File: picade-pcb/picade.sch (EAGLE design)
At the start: 41 parts

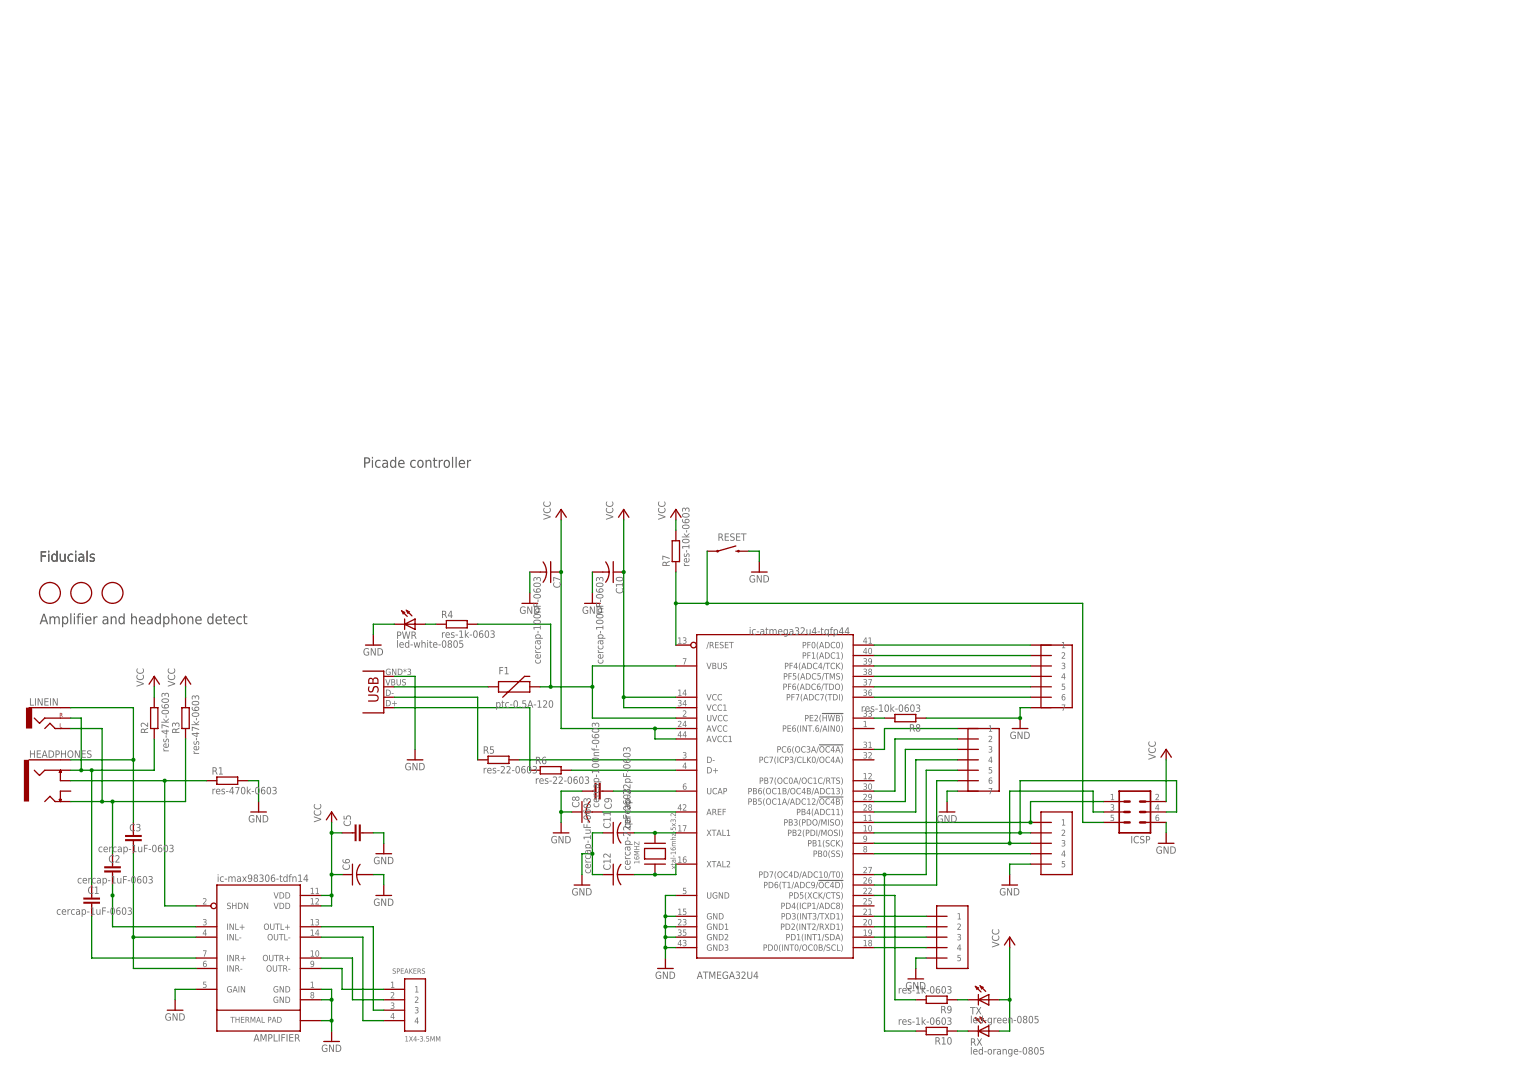
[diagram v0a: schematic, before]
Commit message: v2.00
Production revision of the Picade controller board with matrix scanned
inputs, new amplifier with I2C volume control, and extra audio
filtering.
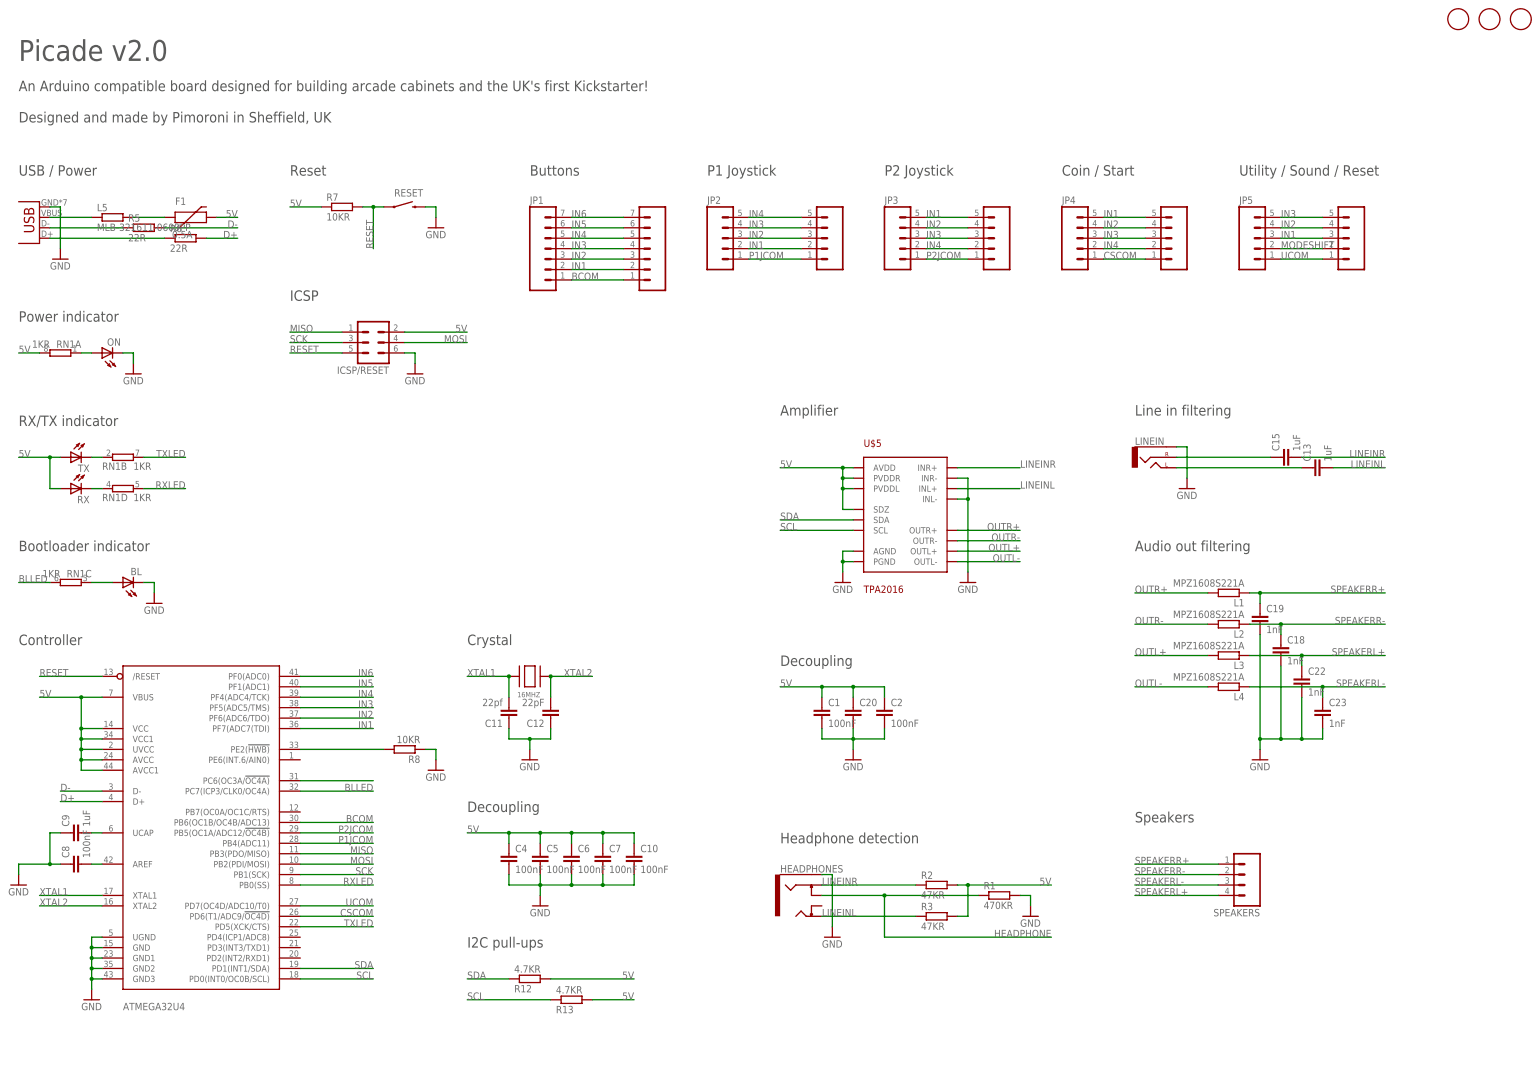
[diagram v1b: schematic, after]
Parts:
- removed AMPLIFIER: ic-max98306-tdfn14, SparkFun-PowerIC:MAX98306ETD+
- removed C3: cercap-1uF-0603, resistor:C-EUC0603K
- removed GPIO: 1X71X7, pimoroni:1X71X7
- removed ICSP: (no value), con-lstb:MA03-2
- removed JOYSTICK: 1X5, adafruit:1X5
- removed PWR: led-white-0805, adafruit:LEDCHIPLED_0805
- removed R10, R4, R9: res-1k-0603, resistor:R-EU_R0603
- added BL, ON: (no value), adafruit:LEDCHIPLED_0805
- added C13, C15: 1uF, resistor:C-EUC0603K
- added C18, C19, C22, C23: 1nF, resistor:C-EUC0603K
- added C20: (no value), resistor:C-EUC0805K
- added C4: 100nF, resistor:C-EUC0603K
- added COIN, P1JOY, P2JOY: 2.54MM-5P-SCREW-TERMINALLOCK, pimoroni:2.54MM-5P-SCREW-TERMINALLOCK
- added ICSP/RESET: (no value), con-lstb:MA03-2
- added JP1: (no value), SparkFun-Connectors:M07LOCK
- added JP2, JP3, JP4, JP5: (no value), SparkFun-Connectors:M05LOCK
- added L1, L2, L3, L4: MPZ1608S221A, resistor:R-EU_R0603
- added L5: MLB-321611-0600PP, rcl:R-EU_R1206
- added R12, R13: 4.7KR, resistor:R-EU_R0603
- added RN1: 1KR, resistor-dil:4R-N0603-ARC
- added U$5: TPA2016, pimoroni:TPA2016D2
- 16MHZ: value xtal-16mhz-5x3.2 -> (none)
- ATMEGA32U4: value ic-atmega32u4-tqfp44 -> ATMEGA32U4-AU; device adafruit:ATMEGA32U4-AU -> pimoroni:ATMEGA32U4-AU
- BUTTONS: value 1X71X7 -> 2.54MM-7P-SCREW-TERMINALLOCK; device pimoroni:1X71X7 -> pimoroni:2.54MM-7P-SCREW-TERMINALLOCK
- C1, C2: value cercap-1uF-0603 -> 100nF
- C10, C6, C7: value cercap-100nF-0603 -> 100nF; device adafruit:C-USC0603K -> resistor:C-EUC0603K
- C11: value cercap-22pF-0603 -> 22pf; device adafruit:C-USC0603K -> resistor:C-EUC0603K
- C12: value cercap-22pF-0603 -> 22pF; device adafruit:C-USC0603K -> resistor:C-EUC0603K
- C5: value cercap-10uF-0805 -> 100nF; device resistor:C-EUC0805K -> resistor:C-EUC0603K
- C8: value cercap-100nf-0603 -> 100nF; device adafruit:C-USC0603K -> resistor:C-EUC0603K
- C9: value cercap-1uF-0603 -> 1uF
- F1: value ptc-0.5A-120 -> 0.5A
- R1: value res-470k-0603 -> 470KR
- R2, R3: value res-47k-0603 -> 47KR
- R5, R6: value res-22-0603 -> 22R
- R7, R8: value res-10k-0603 -> 10KR
- RX: value led-orange-0805 -> (none)
- SPEAKERS: value 1X4-3.5MM -> 2.54MM-4P-SCREW-TERMINALLOCK; device adafruit:1X4-3.5MM -> pimoroni:2.54MM-4P-SCREW-TERMINALLOCK
- TX: value led-green-0805 -> (none)
- U$1, U$2, U$3: value FIDUCIAL -> FIDUCIAL2MM; device adafruit:FIDUCIAL -> pimoroni:FIDUCIAL2MM
- USB: value USB-REVERSE-MICROB -> USB-MICROB; device pimoroni:USB-REVERSE-MICROB -> pimoroni:USB-MICROB
- UTILITY: value 1X5 -> 2.54MM-5P-SCREW-TERMINALLOCK; device adafruit:1X5 -> pimoroni:2.54MM-5P-SCREW-TERMINALLOCK
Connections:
- net N$1 renamed XTAL1
- net N$2 renamed D-
- net N$5 renamed D+
- net N$8 renamed XTAL2
- removed net N$10: ATMEGA32U4.PD5(XCK/CTS), R9.2
- removed net N$13: ATMEGA32U4.PD7(OC4D/ADC10/T0), GPIO.5, R10.2
- removed net N$14: ATMEGA32U4.PB3(PDO/MISO), ICSP.1, JOYSTICK.1
- removed net N$16: ATMEGA32U4.PB1(SCK), ICSP.3, JOYSTICK.3
- removed net N$17: C3.1, HEADPHONES.SLEEVE, LINEIN.SLEEVE
- removed net N$18: ATMEGA32U4.PF0(ADC0), BUTTONS.1
- removed net N$19: ATMEGA32U4.PF1(ADC1), BUTTONS.2
- removed net N$20: ATMEGA32U4.PF4(ADC4/TCK), BUTTONS.3
- removed net N$21: ATMEGA32U4.PF5(ADC5/TMS), BUTTONS.4
- removed net N$22: ATMEGA32U4.PF6(ADC6/TDO), BUTTONS.5
- removed net N$23: ATMEGA32U4.PF7(ADC7(TDI), BUTTONS.6
- removed net N$24: ATMEGA32U4.PD3(INT3/TXD1), UTILITY.1
- removed net N$25: ATMEGA32U4.PD2(INT2/RXD1), UTILITY.2
- removed net N$26: ATMEGA32U4.PD1(INT1/SDA), UTILITY.3
- removed net N$27: ATMEGA32U4.PD0(INT0/OC0B/SCL), UTILITY.4
- removed net N$28: ATMEGA32U4.PB0(SS), JOYSTICK.4
- removed net N$29: ATMEGA32U4.PB5(OC1A/ADC12/!OC4B), GPIO.3
- removed net N$30: ATMEGA32U4.PB6(OC1B/OC4B/ADC13), GPIO.2
- removed net N$31: ATMEGA32U4.PC6(OC3A/!OC4A), GPIO.1
- removed net N$32: AMPLIFIER.INL-, AMPLIFIER.INR-, C3.2
- removed net N$33: ATMEGA32U4.PD6(T1/ADC9/!OC4D), GPIO.6
- removed net N$34: ATMEGA32U4.PB4(ADC11), GPIO.4
- removed net N$35: AMPLIFIER.INL+, C2.2
- removed net N$36: AMPLIFIER.INR+, C1.2
- removed net N$37: C1.1, HEADPHONES.RING, LINEIN.RIGHT, R2.1
- removed net N$38: C2.1, HEADPHONES.TIP, LINEIN.LEFT, R3.1
- removed net N$39: ATMEGA32U4.PB2(PDI/MOSI), ICSP.4, JOYSTICK.2
- removed net N$42: AMPLIFIER.SHDN, HEADPHONES.RSH, R1.1
- removed net N$9: PWR.A, R4.1
- removed net VCC: AMPLIFIER.VDD@1, AMPLIFIER.VDD@2, ATMEGA32U4.AVCC, ATMEGA32U4.AVCC1, ATMEGA32U4.UVCC, ATMEGA32U4.VBUS, ATMEGA32U4.VCC, ATMEGA32U4.VCC1, C10.1, C5.1, C6.1, C7.1, F1.2, ICSP.2, R2.2, R3.2, R4.2, R7.2, RX.A, TX.A
- new net 5V: ATMEGA32U4.AVCC, ATMEGA32U4.AVCC1, ATMEGA32U4.UVCC, ATMEGA32U4.VBUS, ATMEGA32U4.VCC, ATMEGA32U4.VCC1, C1.1, C10.1, C2.1, C20.1, C4.1, C5.1, C6.1, C7.1, F1.2, ICSP/RESET.2, R12.2, R13.2, R2.2, R3.2, R7.1, RN1A.2, RX.A, TX.A, U$5.AVDD, U$5.PVDDL, U$5.PVDDR, U$5.SDZ
- new net BCOM: ATMEGA32U4.PB6(OC1B/OC4B/ADC13), BUTTONS.1, JP1.1
- new net BLLED: ATMEGA32U4.PC7(ICP3/CLK0/OC4A), RN1C.2
- new net CSCOM: ATMEGA32U4.PD6(T1/ADC9/!OC4D), COIN.1, JP4.1
- new net HEADPHONE: ATMEGA32U4.PC6(OC3A/!OC4A), HEADPHONES.RSH, R1.1
- new net IN1: ATMEGA32U4.PF7(ADC7(TDI), BUTTONS.2, COIN.5, JP1.2, JP2.2, JP3.5, JP4.5, JP5.3, P1JOY.2, P2JOY.5, UTILITY.3
- new net IN2: ATMEGA32U4.PF6(ADC6/TDO), BUTTONS.3, COIN.4, JP1.3, JP2.3, JP3.4, JP4.4, JP5.4, P1JOY.3, P2JOY.4, UTILITY.4
- new net IN3: ATMEGA32U4.PF5(ADC5/TMS), BUTTONS.4, COIN.3, JP1.4, JP2.4, JP3.3, JP4.3, JP5.5, P1JOY.4, P2JOY.3, UTILITY.5
- new net IN4: ATMEGA32U4.PF4(ADC4/TCK), BUTTONS.5, COIN.2, JP1.5, JP2.5, JP3.2, JP4.2, P1JOY.5, P2JOY.2
- new net IN5: ATMEGA32U4.PF1(ADC1), BUTTONS.6, JP1.6
- new net IN6: ATMEGA32U4.PF0(ADC0), BUTTONS.7, JP1.7
- new net LINEINL: C13.2, HEADPHONES.TIP, R3.1, U$5.INL+
- new net LINEINR: C15.2, HEADPHONES.RING, R2.1, U$5.INR+
- new net MISO: ATMEGA32U4.PB3(PDO/MISO), ICSP/RESET.1
- new net MODESHIFT: JP5.2, UTILITY.2
- new net MOSI: ATMEGA32U4.PB2(PDI/MOSI), ICSP/RESET.4
- new net N$1: ATMEGA32U4.UCAP, C9.2
- new net N$2: ON.A, RN1A.1
- new net N$7: F1.1, L5.2
- new net P1JCOM: ATMEGA32U4.PB4(ADC11), JP2.1, P1JOY.1
- new net P2JCOM: ATMEGA32U4.PB5(OC1A/ADC12/!OC4B), JP3.1, P2JOY.1
- new net PRELINEINL: C13.1, LINEIN.LEFT
- new net PRELINEINR: C15.1, LINEIN.RIGHT
- new net RXLED: ATMEGA32U4.PB0(SS), RN1D.2
- new net SCK: ATMEGA32U4.PB1(SCK), ICSP/RESET.3
- new net SCL: ATMEGA32U4.PD0(INT0/OC0B/SCL), R13.1, U$5.SCL
- new net SDA: ATMEGA32U4.PD1(INT1/SDA), R12.1, U$5.SDA
- new net SPEAKERL+: C22.1, L3.1, SPEAKERS.4
- new net SPEAKERL-: C23.1, L4.1, SPEAKERS.3
- new net SPEAKERR+: C19.1, L1.1, SPEAKERS.1
- new net SPEAKERR-: C18.1, L2.1, SPEAKERS.2
- new net TXLED: ATMEGA32U4.PD5(XCK/CTS), RN1B.2
- new net UCOM: ATMEGA32U4.PD7(OC4D/ADC10/T0), JP5.1, UTILITY.1
- net GND: now also BL.C, C1.2, C18.2, C19.2, C2.2, C20.2, C22.2, C23.2, C4.2, C9.1, HEADPHONES.SLEEVE, ICSP/RESET.6, LINEIN.SLEEVE, ON.C, U$5.AGND, U$5.INL-, U$5.INR-, U$5.PGND; no longer AMPLIFIER.GAIN, AMPLIFIER.GND@1, AMPLIFIER.GND@2, AMPLIFIER.GND@3, BUTTONS.7, C9.2, GPIO.7, ICSP.6, JOYSTICK.5, PWR.C, UTILITY.5
- net N$11: now also RN1B.1; no longer R9.1
- net N$12: now also RN1D.1; no longer R10.1
- net N$15: now also L5.1; no longer F1.1
- net N$6: now also BL.A, RN1C.1; no longer ATMEGA32U4.UCAP, C9.1
- net OUTL+: now also L3.2, U$5.OUTL+; no longer AMPLIFIER.OUTL+, SPEAKERS.3
- net OUTL-: now also L4.2, U$5.OUTL-; no longer AMPLIFIER.OUTL-, SPEAKERS.4
- net OUTR+: now also L1.2, U$5.OUTR+; no longer AMPLIFIER.OUTR+, SPEAKERS.2
- net OUTR-: now also L2.2, U$5.OUTR-; no longer AMPLIFIER.OUTR-, SPEAKERS.1
- net RESET: now also ICSP/RESET.5, R7.2; no longer ICSP.5, R7.1
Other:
- note added: "Amplifier"
- note added: "An Arduino compatible board designed for building arcade cabinets and the UK's first Kickstarter! Designed and made by Pimoroni in Sheffield, UK"
- note added: "Audio out filtering"
- note added: "Bootloader indicator"
- note added: "Buttons"
- note added: "Coin / Start"
- note added: "Controller"
- note added: "Crystal"
- note added: "Decoupling"
- note added: "Headphone detection"
- note added: "I2C pull-ups"
- note added: "ICSP"
- note added: "Line in filtering"
- note added: "P1 Joystick"
- note added: "P2 Joystick"
- note added: "Picade v2.0"
- note added: "Power indicator"
- note added: "RX/TX indicator"
- note added: "Reset"
- note added: "Speakers"
- note added: "USB / Power"
- note added: "Utility / Sound / Reset"
- note removed: "Amplifier and headphone detect"
- note removed: "Fiducials"
- note removed: "Picade controller"
- moved on the sheet: 16MHZ, ATMEGA32U4, C1, C10, C11, C12, C2, C5, C6, C7, C8, C9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

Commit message: Picade retail board V2.01
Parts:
- U$1, U$2, U$3: value FIDUCIAL2MM -> FIDUCIAL1MM; device pimoroni:FIDUCIAL2MM -> pimoroni:FIDUCIAL1MM
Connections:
- net MODESHIFT: now also ATMEGA32U4.PD4(ICP1/ADC8)
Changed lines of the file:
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@@
 <part name="GND18" library="supply1" deviceset="GND" device=""/>
 <part name="R7" library="resistor" deviceset="R-EU_" device="R0603" value="10KR"/>
-<part name="U$3" library="pimoroni" deviceset="FIDUCIAL" device="2MM"/>
-<part name="U$1" library="pimoroni" deviceset="FIDUCIAL" device="2MM"/>
-<part name="U$2" library="pimoroni" deviceset="FIDUCIAL" device="2MM"/>
+<part name="U$3" library="pimoroni" deviceset="FIDUCIAL" device="1MM" value="FIDUCIAL1MM"/>
+<part name="U$1" library="pimoroni" deviceset="FIDUCIAL" device="1MM" value="FIDUCIAL1MM"/>
+<part name="U$2" library="pimoroni" deviceset="FIDUCIAL" device="1MM" value="FIDUCIAL1MM"/>
 <part name="R8" library="resistor" deviceset="R-EU_" device="R0603" value="10KR"/>
 <part name="HEADPHONES" library="pimoroni" deviceset="AUDIO-JACK2" device="SMD" value="stereo-jack-switched"/>
@@
 <pinref part="UTILITY" gate="G$1" pin="2"/>
 </segment>
-</net>
+<segment>
+<pinref part="ATMEGA32U4" gate="G$1" pin="PD4(ICP1/ADC8)"/>
+<wire x1="99.06" y1="27.94" x2="81.28" y2="27.94" width="0.1524" layer="91"/>
+<label x="99.06" y="27.94" size="1.778" layer="95" rot="MR0"/>
+</segment>
+</net>

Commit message: Prior to amplifier change
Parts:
- C20: value (none) -> 10uF
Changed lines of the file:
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@@
 <part name="C23" library="resistor" deviceset="C-EU" device="C0603K" value="1nF"/>
 <part name="RN1" library="resistor-dil" deviceset="4R-N" device="0603-ARC" value="1KR"/>
-<part name="C20" library="resistor" deviceset="C-EU" device="C0805K"/>
+<part name="C20" library="resistor" deviceset="C-EU" device="C0805K" value="10uF"/>
 <part name="C2" library="resistor" deviceset="C-EU" device="C0603K" value="100nF"/>
 <part name="GND13" library="supply1" deviceset="GND" device=""/>
@@
 <pinref part="ATMEGA32U4" gate="G$1" pin="PC6(OC3A/!OC4A)"/>
 <wire x1="81.28" y1="66.04" x2="99.06" y2="66.04" width="0.1524" layer="91"/>
-</segment>
-</net>
+<label x="99.06" y="66.04" size="1.778" layer="95" rot="MR0"/>
+</segment>
+</net>

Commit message: v1.02
Changed amp to allow for up/down volume control. Better USB signal
routing. Pull-up on MODESHIFT
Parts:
- removed C20: 10uF, resistor:C-EUC0805K
- removed R12, R13: 4.7KR, resistor:R-EU_R0603
- removed U$5: TPA2016, pimoroni:TPA2016D2
- added C14: 0.1uF, resistor:C-EUC0603K
- added C3: 100uF, resistor:CPOL-EU153CLV-0605
- added R4: 47KR, resistor:R-EU_R0603
- added U$4: PAM8407, pimoroni:PAM8407
- C13, C15: value 1uF -> 0.1uF
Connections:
- removed net PRELINEINL: C13.1, LINEIN.LEFT
- removed net PRELINEINR: C15.1, LINEIN.RIGHT
- removed net SCL: ATMEGA32U4.PD0(INT0/OC0B/SCL), R13.1, U$5.SCL
- removed net SDA: ATMEGA32U4.PD1(INT1/SDA), R12.1, U$5.SDA
- new net LIENINLCAP: C13.2, U$4.LINP
- new net LINEINRCAP: C15.2, U$4.RINP
- new net N$9: C14.2, U$4.LINN, U$4.RINN
- new net SHDWN: U$4.SD
- new net VDOWN: ATMEGA32U4.PD1(INT1/SDA), U$4.DOWN
- new net VUP: ATMEGA32U4.PD0(INT0/OC0B/SCL), U$4.UP
- net 5V: now also C3.+, R4.2, U$4.VDD; no longer C20.1, R12.2, R13.2, U$5.AVDD, U$5.PVDDL, U$5.PVDDR, U$5.SDZ
- net BLLED: now also RN1B.2; no longer RN1C.2
- net GND: now also C14.1, C3.-, U$4.GND; no longer C20.2, U$5.AGND, U$5.INL-, U$5.INR-, U$5.PGND
- net LINEINL: now also C13.1, LINEIN.LEFT; no longer C13.2, U$5.INL+
- net LINEINR: now also C15.1, LINEIN.RIGHT; no longer C15.2, U$5.INR+
- net MODESHIFT: now also R4.1
- net N$11: now also RN1C.1; no longer RN1B.1
- net N$6: now also RN1B.1; no longer RN1C.1
- net OUTL+: now also U$4.LOUTP; no longer U$5.OUTL+
- net OUTL-: now also U$4.LOUTN; no longer U$5.OUTL-
- net OUTR+: now also U$4.ROUTP; no longer U$5.OUTR+
- net OUTR-: now also U$4.ROUTN; no longer U$5.OUTR-
- net TXLED: now also RN1C.2; no longer RN1B.2
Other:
- note added: "Modeshift pullup"
- note removed: "I2C pull-ups"
- moved on the sheet: C13, C15, RN1B, RN1C

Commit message: Production candidate
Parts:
- removed COIN, P2JOY, UTILITY: 2.54MM-5P-SCREW-TERMINALLOCK, pimoroni:2.54MM-5P-SCREW-TERMINALLOCK
- removed JP4, JP5: (no value), SparkFun-Connectors:M05LOCK
- removed R4: 47KR, resistor:R-EU_R0603
- added BUTTONS1: 2.54MM-7P-SCREW-TERMINALLOCK, pimoroni:2.54MM-7P-SCREW-TERMINALLOCK
- added C16: 100nF, resistor:C-EUC0805K
- 16MHZ: value (none) -> TSX-3225; device adafruit:XTALNX5032 -> pimoroni:TSX-3225
- C3: value 100uF -> 100nF; device resistor:CPOL-EU153CLV-0605 -> resistor:C-EUC0603K
- JP3: device SparkFun-Connectors:M05LOCK -> SparkFun-Connectors:M07LOCK
- renumbered P1JOY to JOYSTICK
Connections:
- net IN5 renamed BUTTON5
- net IN6 renamed BUTTON6
- net LINEINL renamed LINEINL+
- net LINEINR renamed LINEINR+
- net N$15 renamed VBUS
- removed net BCOM: ATMEGA32U4.PB6(OC1B/OC4B/ADC13), BUTTONS.1, JP1.1
- removed net CSCOM: ATMEGA32U4.PD6(T1/ADC9/!OC4D), COIN.1, JP4.1
- removed net IN1: ATMEGA32U4.PF7(ADC7(TDI), BUTTONS.2, COIN.5, JOYSTICK.2, JP1.2, JP2.2, JP3.5, JP4.5, JP5.3, P2JOY.5, UTILITY.3
- removed net IN2: ATMEGA32U4.PF6(ADC6/TDO), BUTTONS.3, COIN.4, JOYSTICK.3, JP1.3, JP2.3, JP3.4, JP4.4, JP5.4, P2JOY.4, UTILITY.4
- removed net IN3: ATMEGA32U4.PF5(ADC5/TMS), BUTTONS.4, COIN.3, JOYSTICK.4, JP1.4, JP2.4, JP3.3, JP4.3, JP5.5, P2JOY.3, UTILITY.5
- removed net IN4: ATMEGA32U4.PF4(ADC4/TCK), BUTTONS.5, COIN.2, JOYSTICK.5, JP1.5, JP2.5, JP3.2, JP4.2, P2JOY.2
- removed net MODESHIFT: ATMEGA32U4.PD4(ICP1/ADC8), JP5.2, R4.1, UTILITY.2
- removed net P1JCOM: ATMEGA32U4.PB4(ADC11), JOYSTICK.1, JP2.1
- removed net P2JCOM: ATMEGA32U4.PB5(OC1A/ADC12/!OC4B), JP3.1, P2JOY.1
- removed net SHDWN: U$4.SD
- removed net UCOM: ATMEGA32U4.PD7(OC4D/ADC10/T0), JP5.1, UTILITY.1
- new net BUTTON1: ATMEGA32U4.PF7(ADC7(TDI), BUTTONS.2, JP1.2
- new net BUTTON2: ATMEGA32U4.PF6(ADC6/TDO), BUTTONS.3, JP1.3
- new net BUTTON3: ATMEGA32U4.PF5(ADC5/TMS), BUTTONS.4, JP1.4
- new net BUTTON4: ATMEGA32U4.PF4(ADC4/TCK), BUTTONS.5, JP1.5
- new net COIN: ATMEGA32U4.PD4(ICP1/ADC8), BUTTONS1.3, JP3.3
- new net DOWN: ATMEGA32U4.PB4(ADC11), JOYSTICK.3, JP2.3
- new net ENTER: ATMEGA32U4.PD2(INT2/RXD1), BUTTONS1.5, JP3.5
- new net ESCAPE: ATMEGA32U4.PD3(INT3/TXD1), BUTTONS1.4, JP3.4
- new net LEFT: ATMEGA32U4.PB5(OC1A/ADC12/!OC4B), JOYSTICK.4, JP2.4
- new net LINEIN-: C14.1, HEADPHONES.SLEEVE, LINEIN.SLEEVE
- new net RIGHT: ATMEGA32U4.PB6(OC1B/OC4B/ADC13), JOYSTICK.5, JP2.5
- new net START: ATMEGA32U4.PD6(T1/ADC9/!OC4D), BUTTONS1.2, JP3.2
- new net UP: ATMEGA32U4.PD7(OC4D/ADC10/T0), JOYSTICK.2, JP2.2
- new net VOLUMEDOWN: ATMEGA32U4.PD1(INT1/SDA), BUTTONS1.6, JP3.6
- new net VOLUMEUP: ATMEGA32U4.PD0(INT0/OC0B/SCL), BUTTONS1.7, JP3.7
- net 5V: now also C16.1, C3.1, U$4.SD; no longer C3.+, R4.2
- net GND: now also 16MHZ.GND, BUTTONS.1, BUTTONS1.1, C16.2, C3.2, JOYSTICK.1, JP1.1, JP2.1, JP3.1; no longer C14.1, C3.-, HEADPHONES.SLEEVE, LINEIN.SLEEVE
- net VDOWN: now also ATMEGA32U4.PE6(INT.6/AIN0); no longer ATMEGA32U4.PD1(INT1/SDA)
- net VUP: now also ATMEGA32U4.PB7(OC0A/OC1C/RTS); no longer ATMEGA32U4.PD0(INT0/OC0B/SCL)
- net XTAL1: now also 16MHZ.XIN; no longer 16MHZ.P$2
- net XTAL2: now also 16MHZ.XOUT; no longer 16MHZ.P$1
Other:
- note added: "Joystick"
- note removed: "Coin / Start"
- note removed: "Modeshift pullup"
- note removed: "P1 Joystick"
- note removed: "P2 Joystick"
- moved on the sheet: C11, C12

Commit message: New layout - pending silkage!
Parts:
- removed BUTTONS, BUTTONS1: 2.54MM-7P-SCREW-TERMINALLOCK, pimoroni:2.54MM-7P-SCREW-TERMINALLOCK
- removed JOYSTICK: 2.54MM-5P-SCREW-TERMINALLOCK, pimoroni:2.54MM-5P-SCREW-TERMINALLOCK
- removed JP1, JP3: (no value), SparkFun-Connectors:M07LOCK
- removed JP2: (no value), SparkFun-Connectors:M05LOCK
- removed SPEAKERS: 2.54MM-4P-SCREW-TERMINALLOCK, pimoroni:2.54MM-4P-SCREW-TERMINALLOCK
- added U$5: 5-WAY, pimoroni-headers:5-WAY
- added U$6, U$7: 7-WAY, pimoroni-headers:7-WAY
- added U$8: 4-WAY, pimoroni-headers:4-WAY
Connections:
- net BUTTON1: now also U$6.P$7; no longer BUTTONS.2, JP1.2
- net BUTTON2: now also U$6.P$6; no longer BUTTONS.3, JP1.3
- net BUTTON3: now also U$6.P$5; no longer BUTTONS.4, JP1.4
- net BUTTON4: now also U$6.P$4; no longer BUTTONS.5, JP1.5
- net BUTTON5: now also U$6.P$3; no longer BUTTONS.6, JP1.6
- net BUTTON6: now also U$6.P$2; no longer BUTTONS.7, JP1.7
- net COIN: now also U$7.P$3; no longer BUTTONS1.3, JP3.3
- net DOWN: now also U$5.P$4; no longer JOYSTICK.3, JP2.3
- net ENTER: now also U$7.P$5; no longer BUTTONS1.5, JP3.5
- net ESCAPE: now also U$7.P$4; no longer BUTTONS1.4, JP3.4
- net GND: now also U$5.P$1, U$6.P$1, U$7.P$1; no longer BUTTONS.1, BUTTONS1.1, JOYSTICK.1, JP1.1, JP2.1, JP3.1
- net LEFT: now also U$5.P$3; no longer JOYSTICK.4, JP2.4
- net RIGHT: now also U$5.P$2; no longer JOYSTICK.5, JP2.5
- net SPEAKERL+: now also U$8.P$4; no longer SPEAKERS.4
- net SPEAKERL-: now also U$8.P$3; no longer SPEAKERS.3
- net SPEAKERR+: now also U$8.P$1; no longer SPEAKERS.1
- net SPEAKERR-: now also U$8.P$2; no longer SPEAKERS.2
- net START: now also U$7.P$2; no longer BUTTONS1.2, JP3.2
- net UP: now also U$5.P$5; no longer JOYSTICK.2, JP2.2
- net VOLUMEDOWN: now also U$7.P$6; no longer BUTTONS1.6, JP3.6
- net VOLUMEUP: now also U$7.P$7; no longer BUTTONS1.7, JP3.7
